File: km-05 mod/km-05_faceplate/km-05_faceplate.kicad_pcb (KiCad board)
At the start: 4 copper layers, 50.8 x 76.2 mm, 4 parts

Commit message: n
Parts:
- added H1: MountingHole_Pad, MountingHole:MountingHole_2.7mm_M2.5_DIN965_Pad_TopBottom, F.Cu at (107.2, 29.2)
- added H2: MountingHole_Pad, MountingHole:MountingHole_2.7mm_M2.5_DIN965_Pad_TopBottom, F.Cu at (146.8, 29.2)
- added H3: MountingHole_Pad, MountingHole:MountingHole_2.7mm_M2.5_DIN965_Pad_TopBottom, F.Cu at (146.8, 97.8)
- added H4: MountingHole_Pad, MountingHole:MountingHole_2.7mm_M2.5_DIN965_Pad_TopBottom, F.Cu at (107.2, 97.8)
- moved H1 17.6 mm to (127.0, 44.4)
- moved H1 17.6 mm to (127.0, 31.7)
- moved H1 17.6 mm to (127.0, 82.4)
- moved H2 17.6 mm to (127.0, 95.2)
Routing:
- net (no net): track 61.3 -> 7.39 mm, vias 10 -> 0
- net 10: track 0.00 -> 11.7 mm, vias 0 -> 1
- net 1: track 0.00 -> 11.0 mm, vias 0 -> 1
- net unconnected-(H3-Pad1): track 0.00 -> 6.96 mm
- net 2: track 0.00 -> 6.86 mm, vias 0 -> 1
- net 9: track 0.00 -> 5.80 mm, vias 0 -> 1
- net 8: track 0.00 -> 5.75 mm, vias 0 -> 1
- net 5: track 0.00 -> 4.43 mm, vias 0 -> 1
- net 4: track 0.00 -> 4.37 mm, vias 0 -> 1
- net 6: track 0.00 -> 3.94 mm, vias 0 -> 1
- net 3: track 0.00 -> 3.80 mm, vias 0 -> 1
- net 7: track 0.00 -> 3.58 mm, vias 0 -> 1
- added copper zone on F.Cu, net 1
- added copper zone on F.Cu, net 10
- added copper zone on F.Cu, net 2
- added copper zone on F.Cu, net 3
- added copper zone on F.Cu, net 4
- added copper zone on F.Cu, net 5
- added copper zone on F.Cu, net 6
- added copper zone on F.Cu, net 7
- added copper zone on F.Cu, net 8
- added copper zone on F.Cu, net 9
- removed copper zone on F.Cu, net (none)
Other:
- board text added: "MODS"

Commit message: n
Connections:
- H1 pad 1: (no net) -> GND (x2)
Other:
- board text added: "TT0.1"

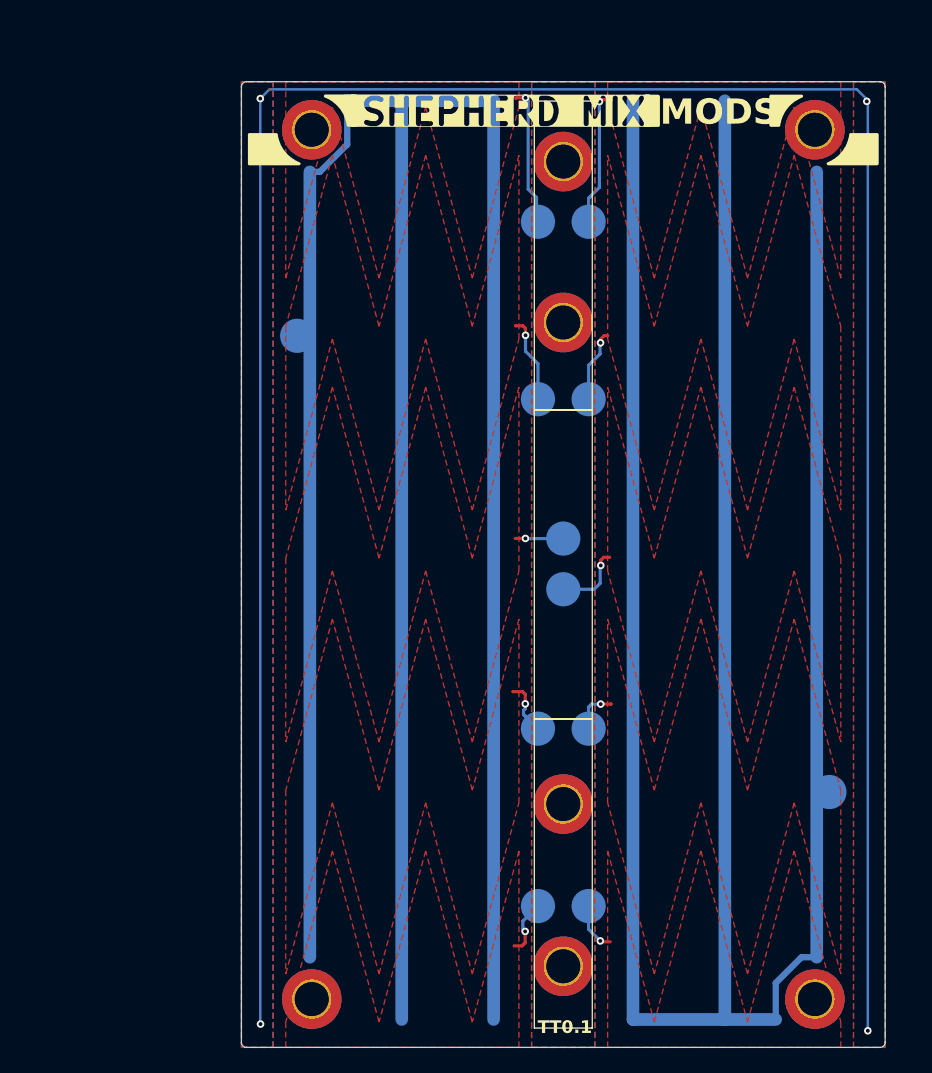
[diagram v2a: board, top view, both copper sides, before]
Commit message: faceplate designs
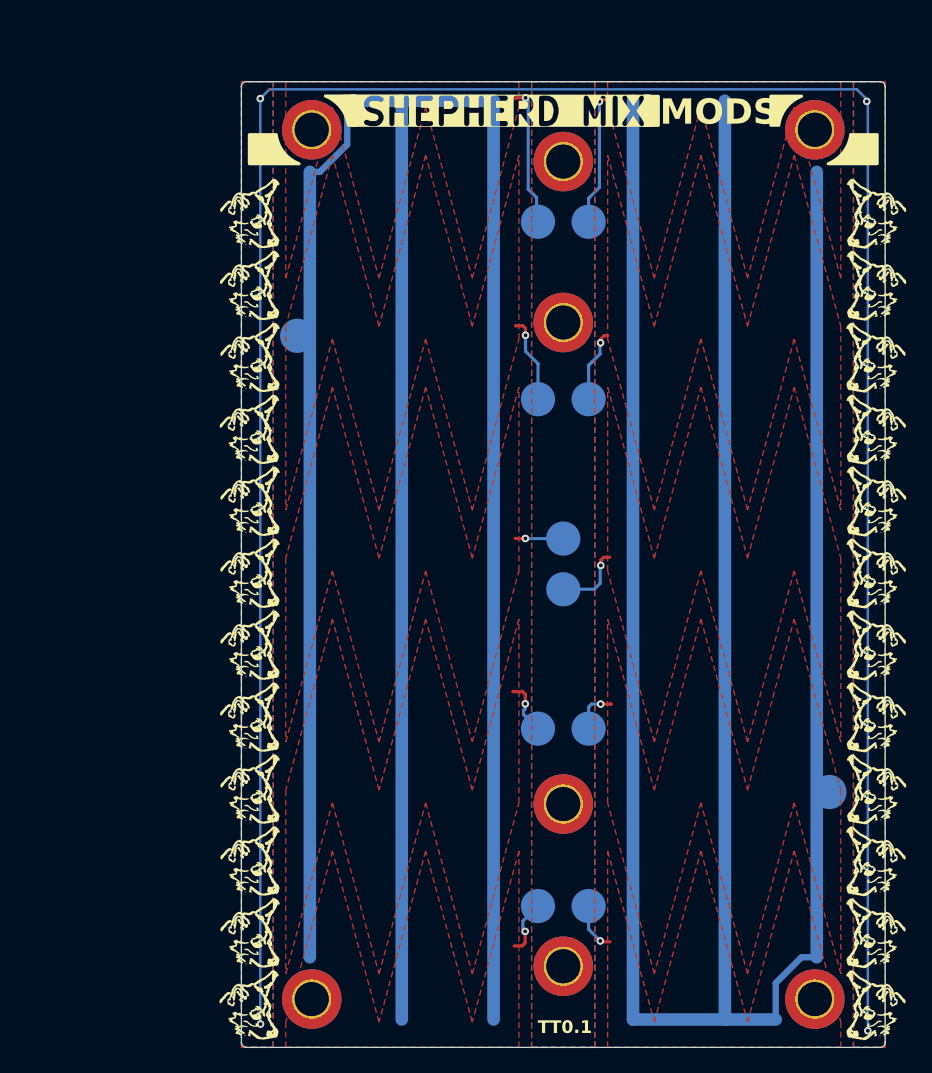
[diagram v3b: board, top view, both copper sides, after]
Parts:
- added G***: LOGO, LOGO, F.Cu at (102.5, 86.7)
- added G***: LOGO, LOGO, F.Cu at (151.4, 47.0)
- added G***: LOGO, LOGO, F.Cu at (151.4, 98.1)
- added G***: LOGO, LOGO, F.Cu at (102.5, 46.9)
- added G***: LOGO, LOGO, F.Cu at (102.5, 41.2)
- added G***: LOGO, LOGO, F.Cu at (102.5, 75.3)
- added G***: LOGO, LOGO, F.Cu at (151.4, 86.8)
- added G***: LOGO, LOGO, F.Cu at (151.5, 58.4)
- added G***: LOGO, LOGO, F.Cu at (102.5, 92.3)
- added G***: LOGO, LOGO, F.Cu at (151.4, 92.5)
- added G***: LOGO, LOGO, F.Cu at (102.5, 98.0)
- added G***: LOGO, LOGO, F.Cu at (102.5, 63.9)
- added G***: LOGO, LOGO, F.Cu at (102.5, 52.6)
- added G***: LOGO, LOGO, F.Cu at (151.5, 41.4)
- added G***: LOGO, LOGO, F.Cu at (151.5, 69.8)
- added G***: LOGO, LOGO, F.Cu at (102.5, 81.0)
- added G***: LOGO, LOGO, F.Cu at (102.5, 58.3)
- added G***: LOGO, LOGO, F.Cu at (102.5, 35.6)
- added G***: LOGO, LOGO, F.Cu at (151.5, 52.7)
- added G***: LOGO, LOGO, F.Cu at (151.5, 75.4)
- added G***: LOGO, LOGO, F.Cu at (151.5, 64.1)
- added G***: LOGO, LOGO, F.Cu at (102.5, 69.6)
- added G***: LOGO, LOGO, F.Cu at (151.5, 81.1)
- added G***: LOGO, LOGO, F.Cu at (151.5, 35.7)

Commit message: production 1
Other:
- copper layers 4 -> 2
